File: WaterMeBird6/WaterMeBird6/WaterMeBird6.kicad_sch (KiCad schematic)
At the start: 14 parts, among them J1 Conn_02x03_Odd_Even, J2 Conn_01x03, Q1 2N3904, SW1 SW_Push, U1 ATtiny85V-10P

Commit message: Added 'thick' version of footprints
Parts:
- D1: footprint LED_THT:LED_D3.0mm -> _Tinker:LED_D3.0mm_Thick
- J2: footprint TerminalBlock_RND:TerminalBlock_RND_205-00002_1x03_P5.00mm_Horizontal -> _Tinker:TerminalBlock_1x03_P5.00mm_Thick
- R1, R2, R3, R4, R6: footprint Resistor_THT:R_Axial_DIN0414_L11.9mm_D4.5mm_P15.24mm_Horizontal -> _Tinker:R_Axial_DIN0309_L9.0mm_D3.2mm_P12.70mm_Horizontal_Thick
- R5: footprint OptoDevice:R_LDR_4.9x4.2mm_P2.54mm_Vertical -> _Tinker:R_LDR_4.9x4.2mm_P2.54mm_Vertical_Thick
- SP1: footprint Buzzer_Beeper:MagneticBuzzer_PUI_AT-0927-TT-6-R -> _Tinker:MagneticBuzzer_Thick
- SW1: footprint Button_Switch_THT:SW_PUSH_6mm_H5mm -> _Tinker:SW_PUSH_6mm_H5mm_Thick
- U1: footprint Package_DIP:DIP-8_W7.62mm -> _Tinker:DIP-8_W7.62mm_Thick
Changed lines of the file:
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@@
       (effects (font (size 1.27 1.27)) (justify left))
     )
-    (property "Footprint" "OptoDevice:R_LDR_4.9x4.2mm_P2.54mm_Vertical" (id 2) (at 269.24 128.27 90)
+    (property "Footprint" "_Tinker:R_LDR_4.9x4.2mm_P2.54mm_Vertical_Thick" (id 2) (at 269.24 128.27 90)
       (effects (font (size 1.27 1.27)) (justify left) hide)
     )
@@
       (effects (font (size 1.27 1.27)) (justify left))
     )
-    (property "Footprint" "Resistor_THT:R_Axial_DIN0414_L11.9mm_D4.5mm_P15.24mm_Horizontal" (id 2) (at 173.482 142.24 90)
+    (property "Footprint" "_Tinker:R_Axial_DIN0309_L9.0mm_D3.2mm_P12.70mm_Horizontal_Thick" (id 2) (at 173.482 142.24 90)
       (effects (font (size 1.27 1.27)) hide)
     )
@@
       (effects (font (size 1.27 1.27)) (justify right))
     )
-    (property "Footprint" "Package_DIP:DIP-8_W7.62mm" (id 2) (at 135.89 86.36 0)
+    (property "Footprint" "_Tinker:DIP-8_W7.62mm_Thick" (id 2) (at 135.89 86.36 0)
       (effects (font (size 1.27 1.27) italic) hide)
     )
@@
       (effects (font (size 1.27 1.27)) (justify left))
     )
-    (property "Footprint" "Resistor_THT:R_Axial_DIN0414_L11.9mm_D4.5mm_P15.24mm_Horizontal" (id 2) (at 266.192 134.62 90)
+    (property "Footprint" "_Tinker:R_Axial_DIN0309_L9.0mm_D3.2mm_P12.70mm_Horizontal_Thick" (id 2) (at 266.192 134.62 90)
       (effects (font (size 1.27 1.27)) hide)
     )
@@
       (effects (font (size 1.27 1.27)) (justify left))
     )
-    (property "Footprint" "TerminalBlock_RND:TerminalBlock_RND_205-00002_1x03_P5.00mm_Horizontal" (id 2) (at 177.8 156.21 0)
+    (property "Footprint" "_Tinker:TerminalBlock_1x03_P5.00mm_Thick" (id 2) (at 177.8 156.21 0)
       (effects (font (size 1.27 1.27)) hide)
     )
@@
       (effects (font (size 1.27 1.27)) (justify left))
     )
-    (property "Footprint" "LED_THT:LED_D3.0mm" (id 2) (at 173.99 68.58 0)
+    (property "Footprint" "_Tinker:LED_D3.0mm_Thick" (id 2) (at 173.99 68.58 0)
       (effects (font (size 1.27 1.27)) hide)
     )
@@
       (effects (font (size 1.27 1.27)) (justify left))
     )
-    (property "Footprint" "Resistor_THT:R_Axial_DIN0414_L11.9mm_D4.5mm_P15.24mm_Horizontal" (id 2) (at 193.802 142.24 90)
+    (property "Footprint" "_Tinker:R_Axial_DIN0309_L9.0mm_D3.2mm_P12.70mm_Horizontal_Thick" (id 2) (at 193.802 142.24 90)
       (effects (font (size 1.27 1.27)) hide)
     )
@@
       (effects (font (size 1.27 1.27)) (justify left))
     )
-    (property "Footprint" "Resistor_THT:R_Axial_DIN0414_L11.9mm_D4.5mm_P15.24mm_Horizontal" (id 2) (at 172.212 58.42 90)
+    (property "Footprint" "_Tinker:R_Axial_DIN0309_L9.0mm_D3.2mm_P12.70mm_Horizontal_Thick" (id 2) (at 172.212 58.42 90)
       (effects (font (size 1.27 1.27)) hide)
     )
@@
       (effects (font (size 1.27 1.27)) (justify left))
     )
-    (property "Footprint" "Buzzer_Beeper:MagneticBuzzer_PUI_AT-0927-TT-6-R" (id 2) (at 248.92 81.28 0)
+    (property "Footprint" "_Tinker:MagneticBuzzer_Thick" (id 2) (at 248.92 81.28 0)
       (effects (font (size 1.27 1.27)) hide)
     )
@@
       (effects (font (size 1.27 1.27)) (justify left))
     )
-    (property "Footprint" "Resistor_THT:R_Axial_DIN0414_L11.9mm_D4.5mm_P15.24mm_Horizontal" (id 2) (at 187.452 83.82 90)
+    (property "Footprint" "_Tinker:R_Axial_DIN0309_L9.0mm_D3.2mm_P12.70mm_Horizontal_Thick" (id 2) (at 187.452 83.82 90)
       (effects (font (size 1.27 1.27)) hide)
     )
@@
     (property "Reference" "SW1" (id 0) (at 199.39 83.82 0))
     (property "Value" "SW_Push" (id 1) (at 199.39 86.36 0))
-    (property "Footprint" "Button_Switch_THT:SW_PUSH_6mm_H5mm" (id 2) (at 199.39 86.36 0)
+    (property "Footprint" "_Tinker:SW_PUSH_6mm_H5mm_Thick" (id 2) (at 199.39 86.36 0)
       (effects (font (size 1.27 1.27)) hide)
     )
@@
     )
     (path "/7efdf5ec-32ec-4d10-ad69-4d14fb60ed0e"
-      (reference "D1") (unit 1) (value "LED") (footprint "LED_THT:LED_D3.0mm")
+      (reference "D1") (unit 1) (value "LED") (footprint "_Tinker:LED_D3.0mm_Thick")
     )
     (path "/d60e94de-6a6e-4464-ba59-4c9a15981d31"
@@
     )
     (path "/3aa13233-e8c2-4503-8382-ffc750bc1ee5"
-      (reference "J2") (unit 1) (value "Conn_01x03") (footprint "TerminalBlock_RND:TerminalBlock_RND_205-00002_1x03_P5.00mm_Horizontal")
+      (reference "J2") (unit 1) (value "Conn_01x03") (footprint "_Tinker:TerminalBlock_1x03_P5.00mm_Thick")
     )
     (path "/a5f5ba7c-ec6a-4c33-9043-b51b8431a50d"
@@
     )
     (path "/f0f7e5fe-5ffe-4196-8f9b-fe35a7f7f218"
-      (reference "R1") (unit 1) (value "10k") (footprint "Resistor_THT:R_Axial_DIN0414_L11.9mm_D4.5mm_P15.24mm_Horizontal")
+      (reference "R1") (unit 1) (value "10k") (footprint "_Tinker:R_Axial_DIN0309_L9.0mm_D3.2mm_P12.70mm_Horizontal_Thick")
     )
     (path "/8cc43f7d-7c32-4277-be2b-ed2d91159862"
-      (reference "R2") (unit 1) (value "10k") (footprint "Resistor_THT:R_Axial_DIN0414_L11.9mm_D4.5mm_P15.24mm_Horizontal")
+      (reference "R2") (unit 1) (value "10k") (footprint "_Tinker:R_Axial_DIN0309_L9.0mm_D3.2mm_P12.70mm_Horizontal_Thick")
     )
     (path "/1b7e6c1b-b87b-4dd9-8a34-1de7740ef1d1"
-      (reference "R3") (unit 1) (value "100") (footprint "Resistor_THT:R_Axial_DIN0414_L11.9mm_D4.5mm_P15.24mm_Horizontal")
+      (reference "R3") (unit 1) (value "100") (footprint "_Tinker:R_Axial_DIN0309_L9.0mm_D3.2mm_P12.70mm_Horizontal_Thick")
     )
     (path "/c353067b-9cbc-44c7-a8f0-608bfe1d3110"
-      (reference "R4") (unit 1) (value "10k") (footprint "Resistor_THT:R_Axial_DIN0414_L11.9mm_D4.5mm_P15.24mm_Horizontal")
+      (reference "R4") (unit 1) (value "10k") (footprint "_Tinker:R_Axial_DIN0309_L9.0mm_D3.2mm_P12.70mm_Horizontal_Thick")
     )
     (path "/088617bf-e2a9-4c38-a67e-7767fabd7b1a"
-      (reference "R5") (unit 1) (value "R_Photo") (footprint "OptoDevice:R_LDR_4.9x4.2mm_P2.54mm_Vertical")
+      (reference "R5") (unit 1) (value "R_Photo") (footprint "_Tinker:R_LDR_4.9x4.2mm_P2.54mm_Vertical_Thick")
     )
     (path "/3412319b-e2f5-4696-b9db-2d012be2a98e"
-      (reference "R6") (unit 1) (value "10k") (footprint "Resistor_THT:R_Axial_DIN0414_L11.9mm_D4.5mm_P15.24mm_Horizontal")
+      (reference "R6") (unit 1) (value "10k") (footprint "_Tinker:R_Axial_DIN0309_L9.0mm_D3.2mm_P12.70mm_Horizontal_Thick")
     )
     (path "/cdd2f27e-1a8b-4b81-9fcc-d4796bc34c95"
-      (reference "SP1") (unit 1) (value "Speaker") (footprint "Buzzer_Beeper:MagneticBuzzer_PUI_AT-0927-TT-6-R")
+      (reference "SP1") (unit 1) (value "Speaker") (footprint "_Tinker:MagneticBuzzer_Thick")
     )
     (path "/f2c0a063-036f-4bdd-8af6-fe0237fca867"
-      (reference "SW1") (unit 1) (value "SW_Push") (footprint "Button_Switch_THT:SW_PUSH_6mm_H5mm")
+      (reference "SW1") (unit 1) (value "SW_Push") (footprint "_Tinker:SW_PUSH_6mm_H5mm_Thick")
     )
     (path "/31bfc3e7-147b-4531-a0c5-e3a305c1647d"
-      (reference "U1") (unit 1) (value "ATtiny85V-10P") (footprint "Package_DIP:DIP-8_W7.62mm")
-    )
-  )
+      (reference "U1") (unit 1) (value "ATtiny85V-10P") (footprint "_Tinker:DIP-8_W7.62mm_Thick")
+    )
+  )

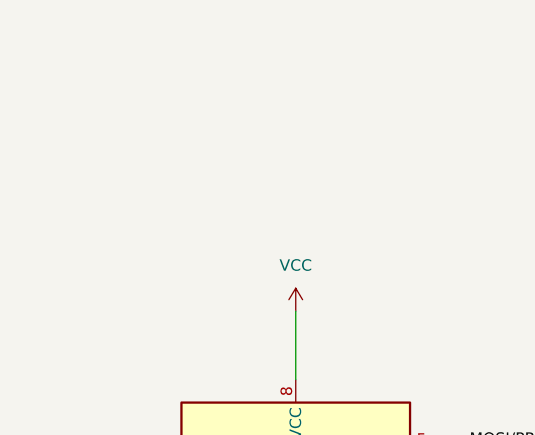
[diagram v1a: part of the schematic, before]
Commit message: added outline and placed
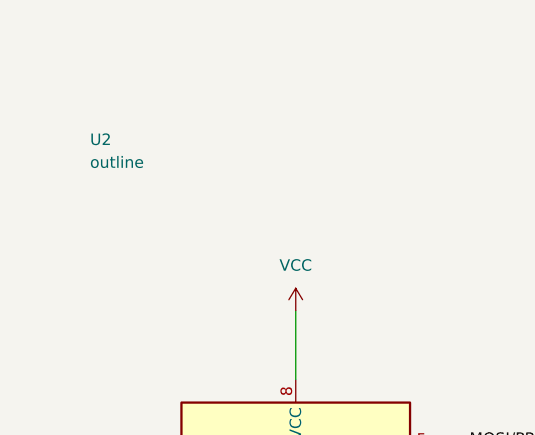
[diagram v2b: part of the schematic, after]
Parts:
- added U2: outline, _Bird:bird_outline, symbol _Tinker:outline
- J1: footprint (none) -> Connector_PinSocket_2.54mm:PinSocket_2x03_P2.54mm_Vertical
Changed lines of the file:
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@@
     (pin "2")
+  )
+  (symbol (lib_id "_Tinker:outline") (at 111.76 45.72 0) (unit 1)
+    (in_bom yes) (on_board yes) (fields_autoplaced)
+    (property "Reference" "U2" (id 0) (at 113.03 44.4499 0)
+      (effects (font (size 1.27 1.27)) (justify left))
+    )
+    (property "Value" "outline" (id 1) (at 113.03 46.9899 0)
+      (effects (font (size 1.27 1.27)) (justify left))
+    )
+    (property "Footprint" "_Bird:bird_outline" (id 2) (at 111.76 45.72 0)
+      (effects (font (size 1.27 1.27)) hide)
+    )
+    (property "Datasheet" "" (id 3) (at 111.76 45.72 0)
+      (effects (font (size 1.27 1.27)) hide)
+    )
   )
   (symbol (lib_id "Connector_Generic:Conn_02x03_Odd_Even") (at 127 142.24 0) (unit 1)
@@
     (property "Reference" "J1" (id 0) (at 128.27 133.35 0))
     (property "Value" "Conn_02x03_Odd_Even" (id 1) (at 128.27 135.89 0))
-    (property "Footprint" "" (id 2) (at 127 142.24 0)
+    (property "Footprint" "Connector_PinSocket_2.54mm:PinSocket_2x03_P2.54mm_Vertical" (id 2) (at 127 142.24 0)
       (effects (font (size 1.27 1.27)) hide)
     )
@@
     )
     (path "/d60e94de-6a6e-4464-ba59-4c9a15981d31"
-      (reference "J1") (unit 1) (value "Conn_02x03_Odd_Even") (footprint "")
+      (reference "J1") (unit 1) (value "Conn_02x03_Odd_Even") (footprint "Connector_PinSocket_2.54mm:PinSocket_2x03_P2.54mm_Vertical")
     )
     (path "/3aa13233-e8c2-4503-8382-ffc750bc1ee5"
@@
       (reference "U1") (unit 1) (value "ATtiny85V-10P") (footprint "_Tinker:DIP-8_W7.62mm_Thick")
     )
+    (path "/d37aab70-b696-4fd1-a736-7958b582b747"
+      (reference "U2") (unit 1) (value "outline") (footprint "_Bird:bird_outline")
+    )
   )
